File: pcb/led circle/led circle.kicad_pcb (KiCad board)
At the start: 2 copper layers, 52.7 x 12.4 mm, 5 parts, among them J1 Conn_01x03_Pin, J2 Conn_01x03_Pin

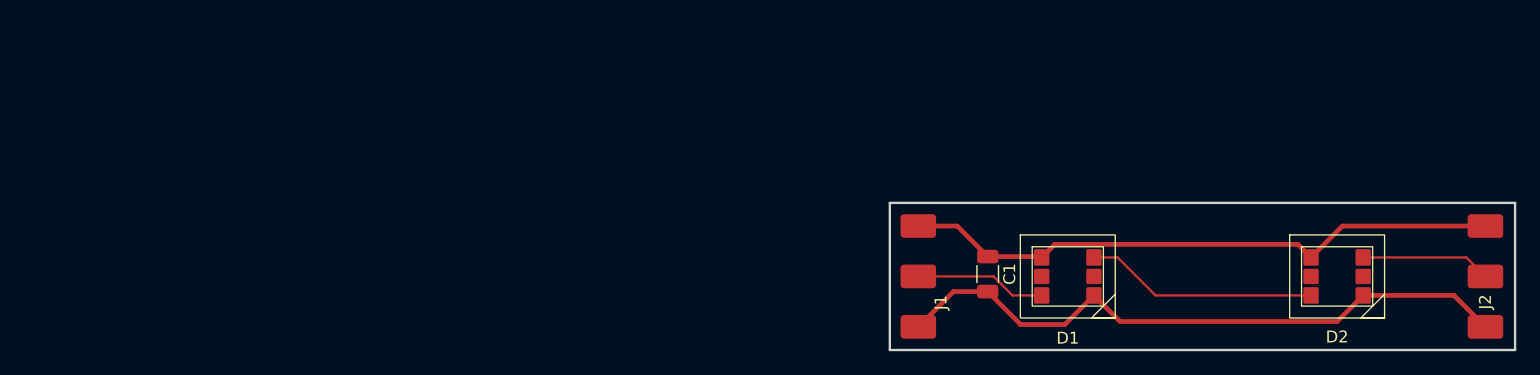
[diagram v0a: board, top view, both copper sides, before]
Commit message: finished all pcbs by adjusting traces acording to 1oz copper weight
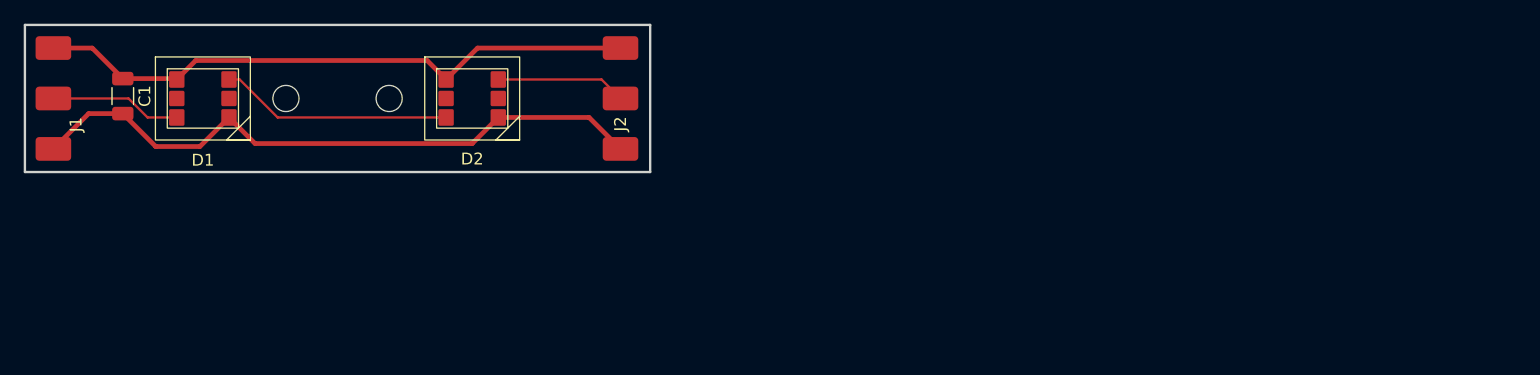
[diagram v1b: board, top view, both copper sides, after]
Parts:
- added REF**: MountingHole_2.2mm_M2, MountingHole:MountingHole_2.2mm_M2, F.Cu at (34.1, 18.2)
- added REF**: MountingHole_2.2mm_M2, MountingHole:MountingHole_2.2mm_M2, F.Cu at (42.8, 18.2)
- moved C1 74.4 mm to (20.4, 18.0)
- moved D1 74.4 mm to (27.1, 18.2)
- moved D2 74.4 mm to (49.8, 18.2)
- moved J1 74.4 mm to (14.5, 18.2)
- moved J2 74.4 mm to (62.3, 18.2)
